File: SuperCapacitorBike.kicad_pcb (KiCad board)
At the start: 2 copper layers, 110.5 x 119.5 mm, 87 parts, among them J1 1988804, J10 1988862, J11 Barrel_Jack_Switch, J12 +5V, J13 1988862, J14 1988817, J2 GND, J3 RX, J4 TX, J5 RESET, J6 1988817, J7 1190363, J8 1190363, J9 1988862, K1 AWHSH105D00G, K2 AWHSH105D00G, Q1 IRFZ44N, Q2 IRFZ44N, Q3 IRFZ44N, Q4 IRFZ44N, Q5 IRFZ44N, Q6 IRFZ44N, Q7 GT065P06T, Q8 IRFZ44N, U1 IR2104, U10 L78L33_TO92, U2 IR2104, U3 IR2104, U4 UCC37324P, U5 MCP23017_SP, U6 ATmega328-P, U7 L7805, U8 ULN2003, U9 MCP4151-xxxx-P

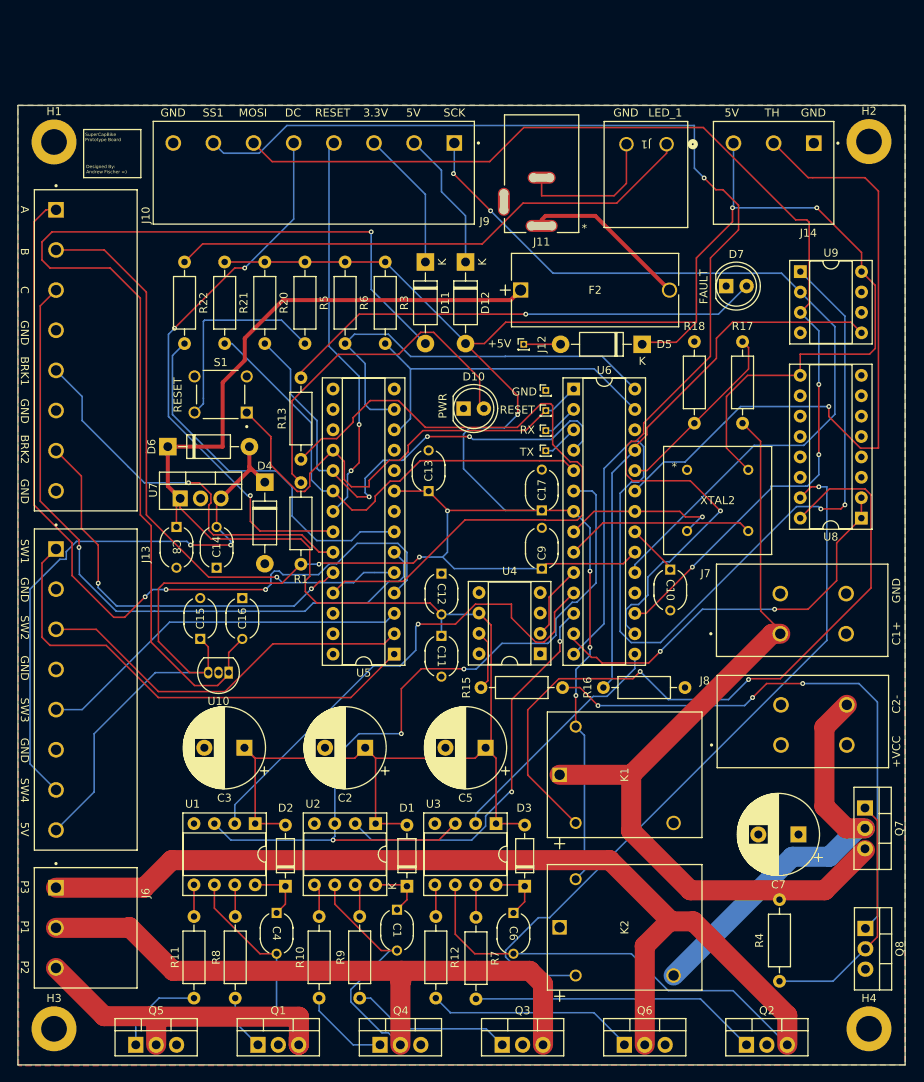
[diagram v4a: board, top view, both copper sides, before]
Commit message: Removed alot of redundent VIAs, added testpoints, cleaned up some traces
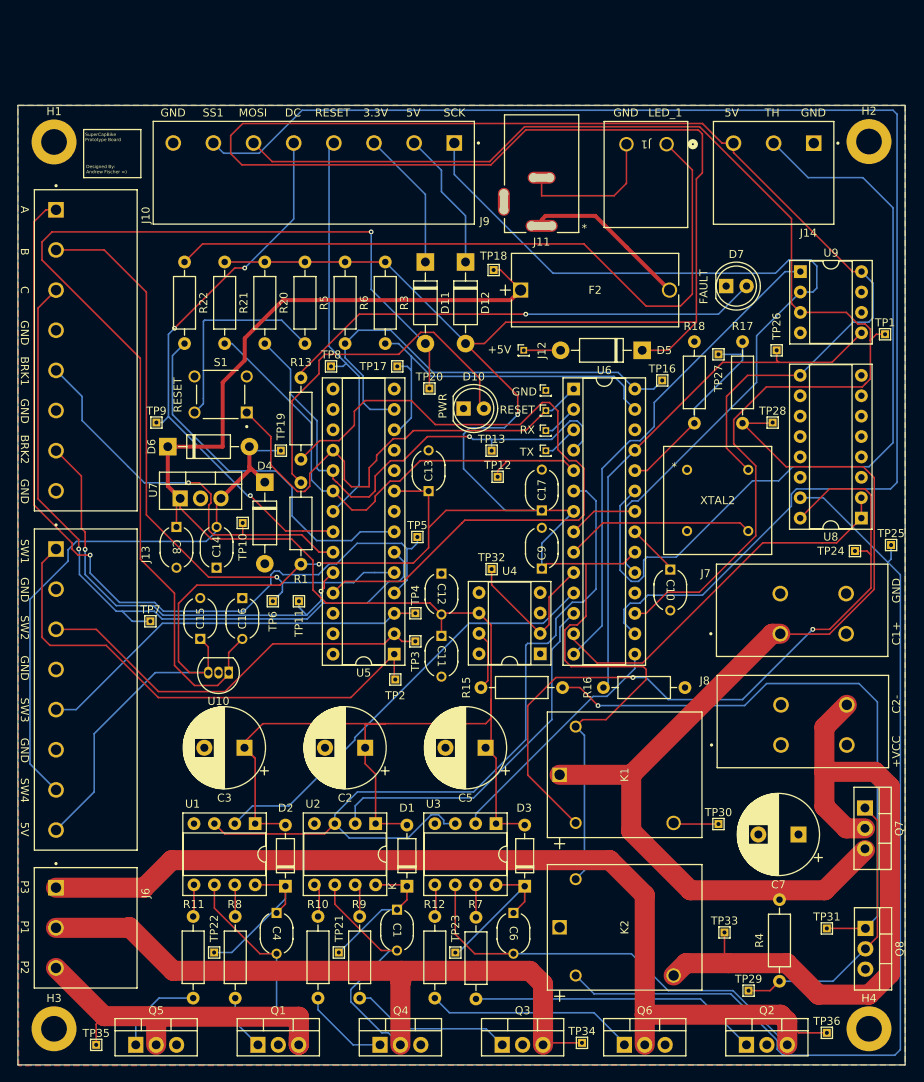
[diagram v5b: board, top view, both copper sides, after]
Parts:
- added TP1: TestPoint, TestPoint:TestPoint_THTPad_1.0x1.0mm_Drill0.5mm, F.Cu at (133.2, 57.5)
- added TP10: TestPoint, TestPoint:TestPoint_THTPad_1.0x1.0mm_Drill0.5mm, F.Cu at (53.2, 81.0)
- added TP11: TestPoint, TestPoint:TestPoint_THTPad_1.0x1.0mm_Drill0.5mm, F.Cu at (60.2, 90.8)
- added TP12: TestPoint, TestPoint:TestPoint_THTPad_1.0x1.0mm_Drill0.5mm, F.Cu at (85.0, 75.2)
- added TP13: TestPoint, TestPoint:TestPoint_THTPad_1.0x1.0mm_Drill0.5mm, F.Cu at (84.2, 72.0)
- added TP16: TestPoint, TestPoint:TestPoint_THTPad_1.0x1.0mm_Drill0.5mm, F.Cu at (105.5, 63.2)
- added TP17: TestPoint, TestPoint:TestPoint_THTPad_1.0x1.0mm_Drill0.5mm, F.Cu at (72.5, 61.5)
- added TP18: TestPoint, TestPoint:TestPoint_THTPad_1.0x1.0mm_Drill0.5mm, F.Cu at (84.5, 49.5)
- added TP19: TestPoint, TestPoint:TestPoint_THTPad_1.0x1.0mm_Drill0.5mm, F.Cu at (58.0, 72.0)
- added TP2: TestPoint, TestPoint:TestPoint_THTPad_1.0x1.0mm_Drill0.5mm, F.Cu at (72.2, 100.5)
- added TP20: TestPoint, TestPoint:TestPoint_THTPad_1.0x1.0mm_Drill0.5mm, F.Cu at (76.5, 64.2)
- added TP21: TestPoint, TestPoint:TestPoint_THTPad_1.0x1.0mm_Drill0.5mm, F.Cu at (65.2, 134.5)
- added TP22: TestPoint, TestPoint:TestPoint_THTPad_1.0x1.0mm_Drill0.5mm, F.Cu at (49.7, 134.5)
- added TP23: TestPoint, TestPoint:TestPoint_THTPad_1.0x1.0mm_Drill0.5mm, F.Cu at (79.7, 134.5)
- added TP24: TestPoint, TestPoint:TestPoint_THTPad_1.0x1.0mm_Drill0.5mm, F.Cu at (129.5, 84.5)
- added TP25: TestPoint, TestPoint:TestPoint_THTPad_1.0x1.0mm_Drill0.5mm, F.Cu at (134.0, 83.8)
- added TP26: TestPoint, TestPoint:TestPoint_THTPad_1.0x1.0mm_Drill0.5mm, F.Cu at (119.8, 59.5)
- added TP27: TestPoint, TestPoint:TestPoint_THTPad_1.0x1.0mm_Drill0.5mm, F.Cu at (112.5, 60.0)
- added TP28: TestPoint, TestPoint:TestPoint_THTPad_1.0x1.0mm_Drill0.5mm, F.Cu at (119.2, 68.5)
- added TP29: TestPoint, TestPoint:TestPoint_THTPad_1.0x1.0mm_Drill0.5mm, F.Cu at (116.2, 139.2)
- added TP3: TestPoint, TestPoint:TestPoint_THTPad_1.0x1.0mm_Drill0.5mm, F.Cu at (74.8, 95.8)
- added TP30: TestPoint, TestPoint:TestPoint_THTPad_1.0x1.0mm_Drill0.5mm, F.Cu at (112.5, 118.5)
- added TP31: TestPoint, TestPoint:TestPoint_THTPad_1.0x1.0mm_Drill0.5mm, F.Cu at (126.0, 131.5)
- added TP32: TestPoint, TestPoint:TestPoint_THTPad_1.0x1.0mm_Drill0.5mm, F.Cu at (84.2, 86.8)
- added TP33: TestPoint, TestPoint:TestPoint_THTPad_1.0x1.0mm_Drill0.5mm, F.Cu at (113.2, 132.0)
- added TP34: TestPoint, TestPoint:TestPoint_THTPad_1.0x1.0mm_Drill0.5mm, F.Cu at (95.5, 145.8)
- added TP35: TestPoint, TestPoint:TestPoint_THTPad_1.0x1.0mm_Drill0.5mm, F.Cu at (35.0, 146.0)
- added TP36: TestPoint, TestPoint:TestPoint_THTPad_1.0x1.0mm_Drill0.5mm, F.Cu at (126.0, 144.5)
- added TP4: TestPoint, TestPoint:TestPoint_THTPad_1.0x1.0mm_Drill0.5mm, F.Cu at (74.8, 92.2)
- added TP5: TestPoint, TestPoint:TestPoint_THTPad_1.0x1.0mm_Drill0.5mm, F.Cu at (75.0, 82.8)
- added TP6: TestPoint, TestPoint:TestPoint_THTPad_1.0x1.0mm_Drill0.5mm, F.Cu at (57.0, 90.8)
- added TP7: TestPoint, TestPoint:TestPoint_THTPad_1.0x1.0mm_Drill0.5mm, F.Cu at (41.8, 93.2)
- added TP8: TestPoint, TestPoint:TestPoint_THTPad_1.0x1.0mm_Drill0.5mm, F.Cu at (64.2, 61.5)
- added TP9: TestPoint, TestPoint:TestPoint_THTPad_1.0x1.0mm_Drill0.5mm, F.Cu at (42.5, 68.5)
- moved D5 0.75 mm to (103.0, 59.5)
- moved J12 0.75 mm to (88.2, 59.5)
- moved R10 0.14 mm to (62.6, 140.2)
- moved R12 0.12 mm to (77.2, 130.0)
- moved R11 0.11 mm to (47.1, 140.2)
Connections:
- U6 pad 18: MISO -> unconnected-(U6-PB4-Pad18)
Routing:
- net +5V: track 387.1 -> 512.1 mm, vias 9 -> 2
- net SS2: track 123.6 -> 61.2 mm, vias 2 -> 0
- net C2-: track 51.4 -> 86.5 mm
- net RELAY_2: track 89.5 -> 123.4 mm, vias 1 -> 0
- net SS1: track 149.5 -> 179.0 mm, vias 2 -> 0
- net C1+: track 103.9 -> 126.9 mm
- net /Motor Controller/LED_1: track 66.8 -> 88.0 mm
- net MOSI: track 139.9 -> 158.4 mm, vias 3 -> 0
- net /Motor Controller/TH_DATA: track 85.1 -> 101.0 mm, vias 1 -> 0
- net +12V: track 229.4 -> 244.3 mm
- net Net-(D2-K): track 7.62 -> 20.8 mm
- net Net-(D3-K): track 7.55 -> 19.6 mm
- net GND: track 38.4 -> 27.1 mm, vias 1 -> 0
- net MOS_DRIVER: track 9.31 -> 19.8 mm
- net Net-(D1-K): track 7.41 -> 16.9 mm
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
